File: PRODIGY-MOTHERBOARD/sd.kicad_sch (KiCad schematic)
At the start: 8 parts, among them J21 DM3BT-DSF-PEJS/C, Q2 DMP2045U-7, U17 IP4252CZ16

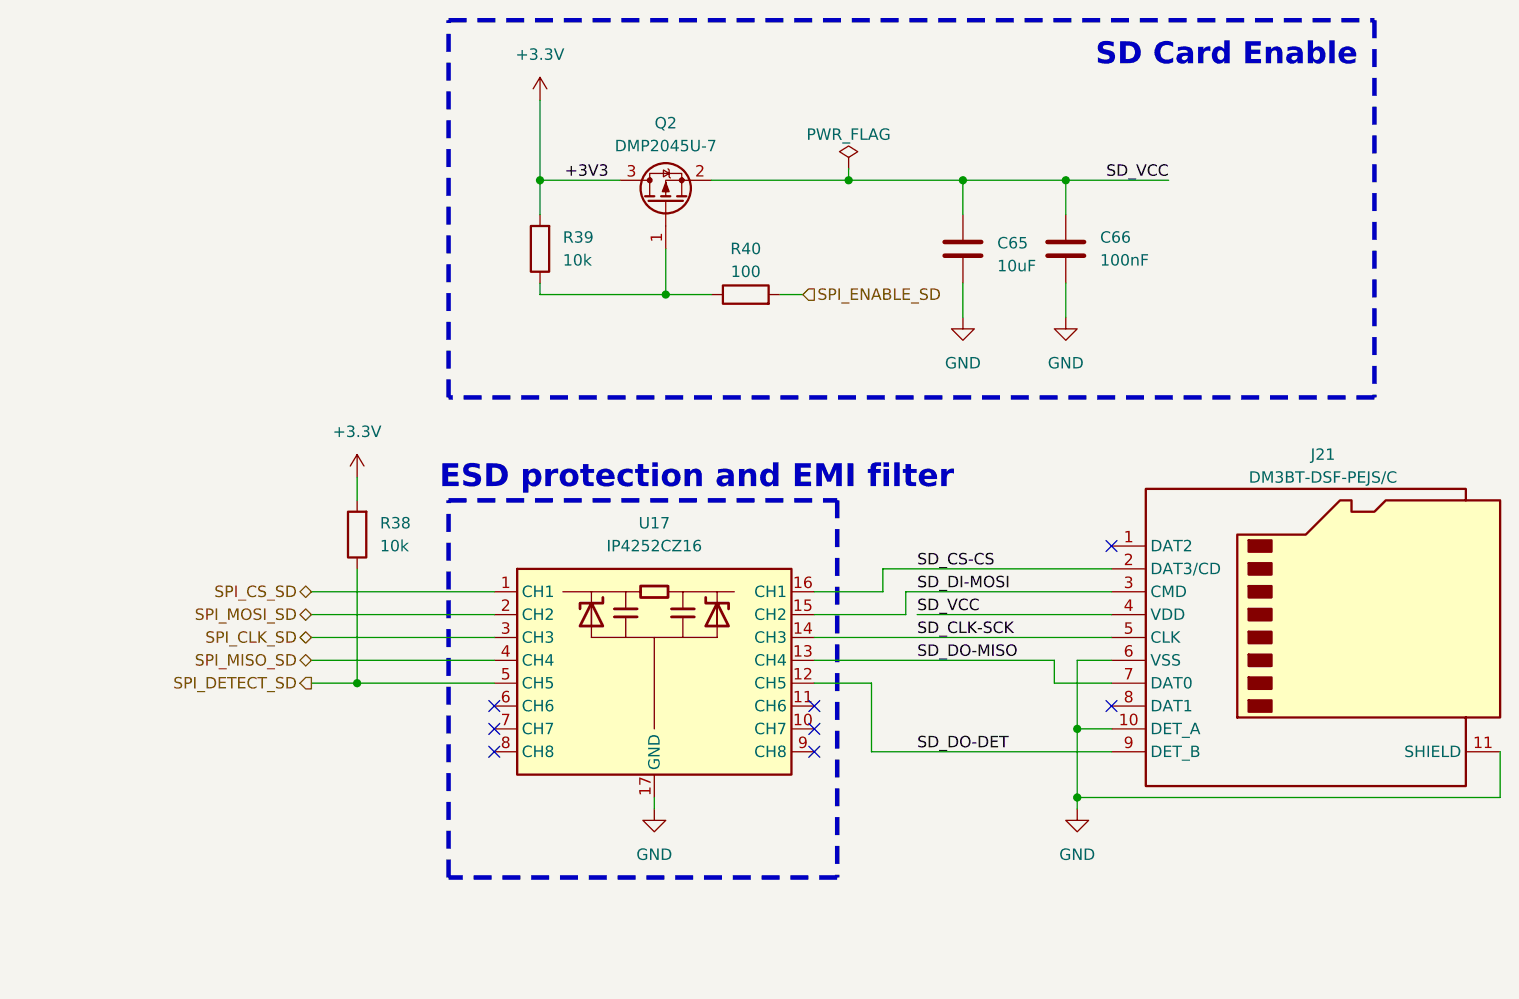
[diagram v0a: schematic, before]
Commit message: MBT Schematic improved
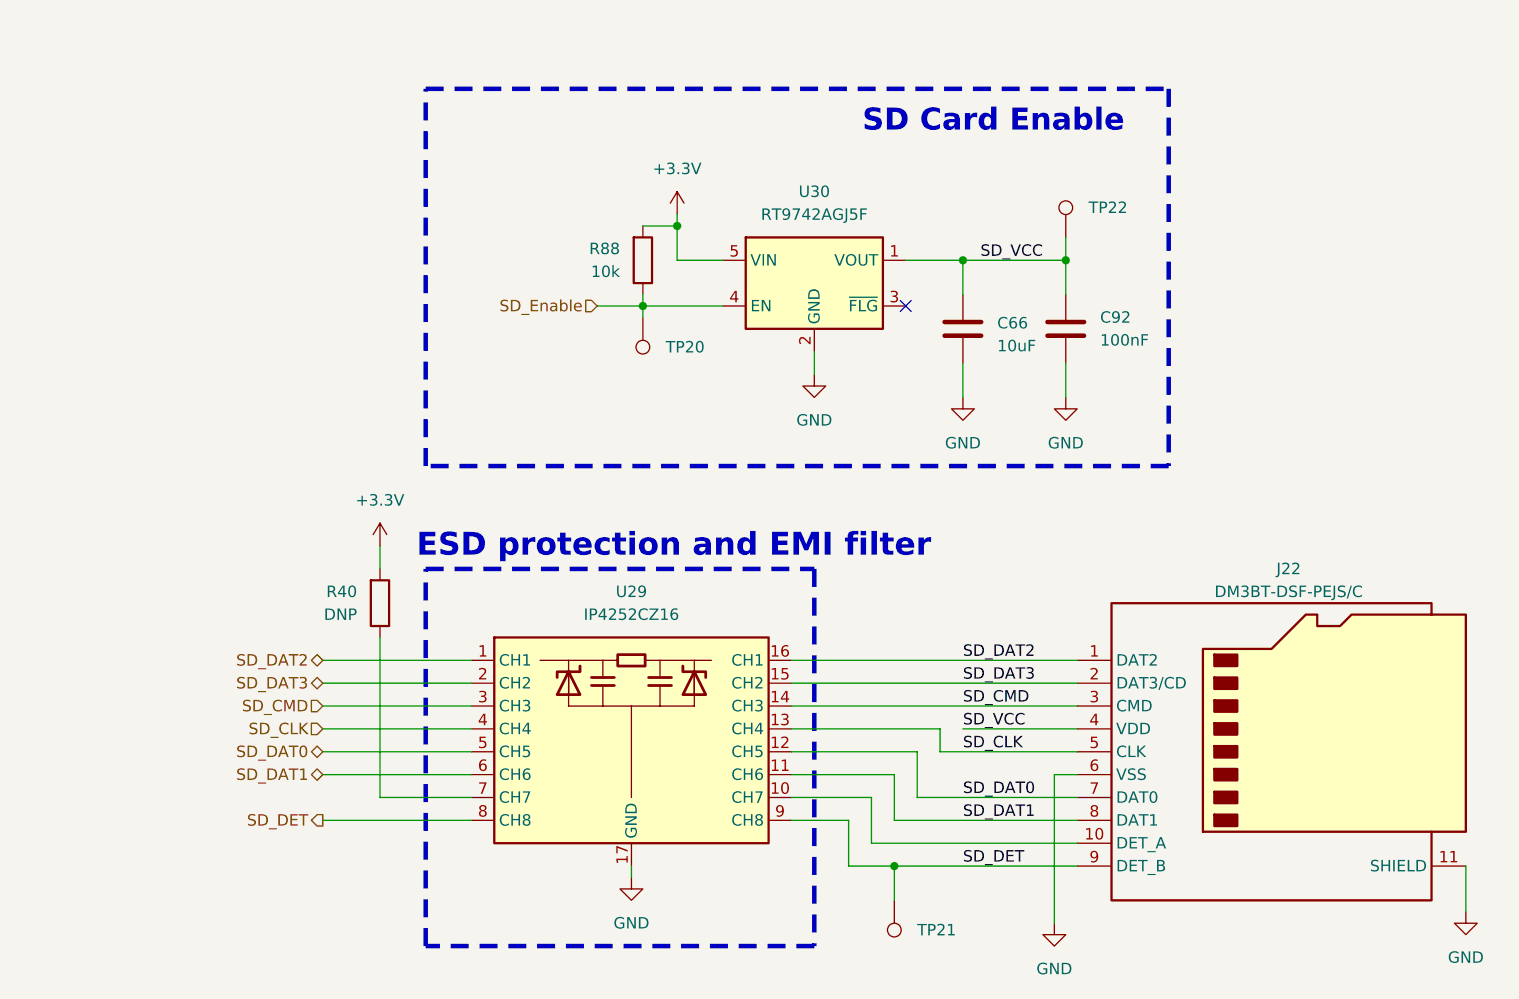
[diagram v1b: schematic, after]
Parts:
- removed C65: 10uF, Capacitor_SMD:C_1206_3216Metric, symbol Device:C
- removed J21: DM3BT-DSF-PEJS/C, Connector_Card:microSD_HC_Hirose_DM3BT-DSF-PEJS, symbol Connector:Micro_SD_Card_Det2
- removed Q2: DMP2045U-7, Package_TO_SOT_SMD:SOT-23, symbol Transistor_FET:IRLML6402
- removed R38, R39: 10k, Resistor_SMD:R_0603_1608Metric, symbol Device:R
- removed U17: IP4252CZ16, Package_SON:Nexperia_HUSON-16_USON-16-1EP_1.35x3.3mm_P0.4mm_EP0.4x2.8mm, symbol Power_Protection:IP4252CZ16
- added C92: 100nF, Capacitor_SMD:C_0805_2012Metric, symbol Device:C
- added J22: DM3BT-DSF-PEJS/C, Connector_Card:microSD_HC_Hirose_DM3BT-DSF-PEJS, symbol Connector:Micro_SD_Card_Det2
- added R88: 10k, Resistor_SMD:R_0603_1608Metric, symbol Device:R
- added TP20, TP21, TP22: ~, TestPoint:TestPoint_Pad_D3.0mm, symbol Connector:TestPoint
- added U29: IP4252CZ16, Package_SON:Nexperia_HUSON-16_USON-16-1EP_1.35x3.3mm_P0.4mm_EP0.4x2.8mm, symbol Power_Protection:IP4252CZ16
- added U30: RT9742AGJ5F, Package_TO_SOT_SMD:TSOT-23-5, symbol Power_Management:RT9742AGJ5F
- C66: value 100nF -> 10uF; footprint Capacitor_SMD:C_0805_2012Metric -> Capacitor_SMD:C_1206_3216Metric
- R40: value 100 -> DNP
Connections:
- net SPI_ENABLE_SD is gone; now on net +3.3V: R40.2
- net +3.3V: now also R88.2, U30.5 (VIN)
- net GND: now also C92.2, J22.11 (SHIELD), J22.6 (VSS), U29.17 (GND), U30.2 (GND)
- net SD_VCC: now also C92.1, J22.4 (VDD), TP22.1, U30.1 (VOUT)
- net at R40.1: now also U29.7 (CH7)
- new net: J22.10 (DET_A), U29.10 (CH7)
- new net SD_CLK: J22.5 (CLK), U29.13 (CH4), U29.4 (CH4)
- new net SD_CMD: J22.3 (CMD), U29.14 (CH3), U29.3 (CH3)
- new net SD_DAT0: J22.7 (DAT0), U29.12 (CH5), U29.5 (CH5)
- new net SD_DAT1: J22.8 (DAT1), U29.11 (CH6), U29.6 (CH6)
- new net SD_DAT2: J22.1 (DAT2), U29.1 (CH1), U29.16 (CH1)
- new net SD_DAT3: J22.2 (DAT3/CD), U29.15 (CH2), U29.2 (CH2)
- new net SD_DET: J22.9 (DET_B), TP21.1, U29.8 (CH8), U29.9 (CH8)
- new net SD_Enable: R88.1, TP20.1, U30.4 (EN)
- no-connect marks 8 -> 1

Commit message: schematic v0.2 finalized
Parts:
- renumbered C66 to C89, C92 to C90, J22 to J21, R40 to R85, R88 to R86, TP20 to TP17, TP21 to TP18, TP22 to TP19, U29 to U27, U30 to U28
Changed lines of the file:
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@@
 		(dnp no)
 		(fields_autoplaced yes)
-		(property "Reference" "U29"
+		(property "Reference" "U27"
 			(at 120.65 104.14 0)
 			(effects
@@
 			(project "PRODIGY-MOTHERBOARD"
 				(path "/f1c25860-8989-4190-bd24-2491d23ca7d9/20646931-b26f-4e3f-9f16-a00d92b20b98"
-					(reference "U29")
+					(reference "U27")
 					(unit 1)
 				)
@@
 		(on_board yes)
 		(dnp no)
-		(property "Reference" "TP21"
+		(property "Reference" "TP18"
 			(at 152.4 141.7319 0)
 			(effects
@@
 			(project "PRODIGY-MOTHERBOARD"
 				(path "/f1c25860-8989-4190-bd24-2491d23ca7d9/20646931-b26f-4e3f-9f16-a00d92b20b98"
-					(reference "TP21")
+					(reference "TP18")
 					(unit 1)
 				)
@@
 		(dnp no)
 		(fields_autoplaced yes)
-		(property "Reference" "#PWR0253"
+		(property "Reference" "#PWR0249"
 			(at 120.65 142.24 0)
 			(effects
@@
 			(project "PRODIGY-MOTHERBOARD"
 				(path "/f1c25860-8989-4190-bd24-2491d23ca7d9/20646931-b26f-4e3f-9f16-a00d92b20b98"
-					(reference "#PWR0253")
+					(reference "#PWR0249")
 					(unit 1)
 				)
@@
 		(on_board yes)
 		(dnp no)
-		(property "Reference" "R88"
+		(property "Reference" "R86"
 			(at 119.38 66.0399 0)
 			(effects
@@
 			(project "PRODIGY-MOTHERBOARD"
 				(path "/f1c25860-8989-4190-bd24-2491d23ca7d9/20646931-b26f-4e3f-9f16-a00d92b20b98"
-					(reference "R88")
+					(reference "R86")
 					(unit 1)
 				)
@@
 		(dnp no)
 		(fields_autoplaced yes)
-		(property "Reference" "#PWR0256"
+		(property "Reference" "#PWR0252"
 			(at 157.48 88.9 0)
 			(effects
@@
 			(project "PRODIGY-MOTHERBOARD"
 				(path "/f1c25860-8989-4190-bd24-2491d23ca7d9/20646931-b26f-4e3f-9f16-a00d92b20b98"
-					(reference "#PWR0256")
+					(reference "#PWR0252")
 					(unit 1)
 				)
@@
 		(dnp no)
 		(fields_autoplaced yes)
-		(property "Reference" "U30"
+		(property "Reference" "U28"
 			(at 140.97 59.69 0)
 			(effects
@@
 			(project "PRODIGY-MOTHERBOARD"
 				(path "/f1c25860-8989-4190-bd24-2491d23ca7d9/20646931-b26f-4e3f-9f16-a00d92b20b98"
-					(reference "U30")
+					(reference "U28")
 					(unit 1)
 				)
@@
 		(dnp no)
 		(fields_autoplaced yes)
-		(property "Reference" "#PWR0252"
+		(property "Reference" "#PWR0248"
 			(at 92.71 102.87 0)
 			(effects
@@
 			(project "PRODIGY-MOTHERBOARD"
 				(path "/f1c25860-8989-4190-bd24-2491d23ca7d9/20646931-b26f-4e3f-9f16-a00d92b20b98"
-					(reference "#PWR0252")
+					(reference "#PWR0248")
 					(unit 1)
 				)
@@
 		(dnp no)
 		(fields_autoplaced yes)
-		(property "Reference" "TP22"
+		(property "Reference" "TP19"
 			(at 171.45 61.4679 0)
 			(effects
@@
 			(project "PRODIGY-MOTHERBOARD"
 				(path "/f1c25860-8989-4190-bd24-2491d23ca7d9/20646931-b26f-4e3f-9f16-a00d92b20b98"
-					(reference "TP22")
+					(reference "TP19")
 					(unit 1)
 				)
@@
 		(dnp no)
 		(fields_autoplaced yes)
-		(property "Reference" "#PWR0254"
+		(property "Reference" "#PWR0250"
 			(at 125.73 66.04 0)
 			(effects
@@
 			(project "PRODIGY-MOTHERBOARD"
 				(path "/f1c25860-8989-4190-bd24-2491d23ca7d9/20646931-b26f-4e3f-9f16-a00d92b20b98"
-					(reference "#PWR0254")
+					(reference "#PWR0250")
 					(unit 1)
 				)
@@
 		(dnp no)
 		(fields_autoplaced yes)
-		(property "Reference" "C66"
+		(property "Reference" "C89"
 			(at 161.29 74.295 0)
 			(effects
@@
 			(project "PRODIGY-MOTHERBOARD"
 				(path "/f1c25860-8989-4190-bd24-2491d23ca7d9/20646931-b26f-4e3f-9f16-a00d92b20b98"
-					(reference "C66")
+					(reference "C89")
 					(unit 1)
 				)
@@
 		(dnp no)
 		(fields_autoplaced yes)
-		(property "Reference" "#PWR0258"
+		(property "Reference" "#PWR0254"
 			(at 168.91 88.9 0)
 			(effects
@@
 			(project "PRODIGY-MOTHERBOARD"
 				(path "/f1c25860-8989-4190-bd24-2491d23ca7d9/20646931-b26f-4e3f-9f16-a00d92b20b98"
-					(reference "#PWR0258")
+					(reference "#PWR0254")
 					(unit 1)
 				)
@@
 		(on_board yes)
 		(dnp no)
-		(property "Reference" "TP20"
+		(property "Reference" "TP17"
 			(at 124.46 76.9621 0)
 			(effects
@@
 			(project "PRODIGY-MOTHERBOARD"
 				(path "/f1c25860-8989-4190-bd24-2491d23ca7d9/20646931-b26f-4e3f-9f16-a00d92b20b98"
-					(reference "TP20")
+					(reference "TP17")
 					(unit 1)
 				)
@@
 		(dnp no)
 		(fields_autoplaced yes)
-		(property "Reference" "#PWR0257"
+		(property "Reference" "#PWR0253"
 			(at 167.64 147.32 0)
 			(effects
@@
 			(project "PRODIGY-MOTHERBOARD"
 				(path "/f1c25860-8989-4190-bd24-2491d23ca7d9/20646931-b26f-4e3f-9f16-a00d92b20b98"
-					(reference "#PWR0257")
+					(reference "#PWR0253")
 					(unit 1)
 				)
@@
 		(on_board yes)
 		(dnp no)
-		(property "Reference" "J22"
+		(property "Reference" "J21"
 			(at 193.675 101.6 0)
 			(effects
@@
 			(project "PRODIGY-MOTHERBOARD"
 				(path "/f1c25860-8989-4190-bd24-2491d23ca7d9/20646931-b26f-4e3f-9f16-a00d92b20b98"
-					(reference "J22")
+					(reference "J21")
 					(unit 1)
 				)
@@
 		(dnp no)
 		(fields_autoplaced yes)
-		(property "Reference" "#PWR0255"
+		(property "Reference" "#PWR0251"
 			(at 140.97 86.36 0)
 			(effects
@@
 			(project "PRODIGY-MOTHERBOARD"
 				(path "/f1c25860-8989-4190-bd24-2491d23ca7d9/20646931-b26f-4e3f-9f16-a00d92b20b98"
-					(reference "#PWR0255")
+					(reference "#PWR0251")
 					(unit 1)
 				)
@@
 		(on_board yes)
 		(dnp no)
-		(property "Reference" "R40"
+		(property "Reference" "R85"
 			(at 90.17 104.1399 0)
 			(effects
@@
 			(project "PRODIGY-MOTHERBOARD"
 				(path "/f1c25860-8989-4190-bd24-2491d23ca7d9/20646931-b26f-4e3f-9f16-a00d92b20b98"
-					(reference "R40")
+					(reference "R85")
 					(unit 1)
 				)
@@
 		(dnp no)
 		(fields_autoplaced yes)
-		(property "Reference" "#PWR0259"
+		(property "Reference" "#PWR0255"
 			(at 213.36 146.05 0)
 			(effects
@@
 			(project "PRODIGY-MOTHERBOARD"
 				(path "/f1c25860-8989-4190-bd24-2491d23ca7d9/20646931-b26f-4e3f-9f16-a00d92b20b98"
-					(reference "#PWR0259")
+					(reference "#PWR0255")
 					(unit 1)
 				)
@@
 		(dnp no)
 		(fields_autoplaced yes)
-		(property "Reference" "C92"
+		(property "Reference" "C90"
 			(at 172.72 73.6599 0)
 			(effects
@@
 			(project "PRODIGY-MOTHERBOARD"
 				(path "/f1c25860-8989-4190-bd24-2491d23ca7d9/20646931-b26f-4e3f-9f16-a00d92b20b98"
-					(reference "C92")
-					(unit 1)
-				)
+					(reference "C90")
+					(unit 1)
+				)

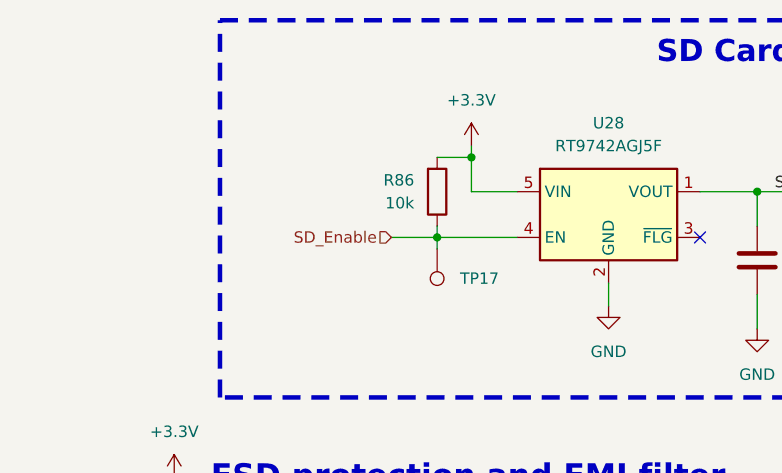
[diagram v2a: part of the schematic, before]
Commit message: Motherboard footprints assigned.
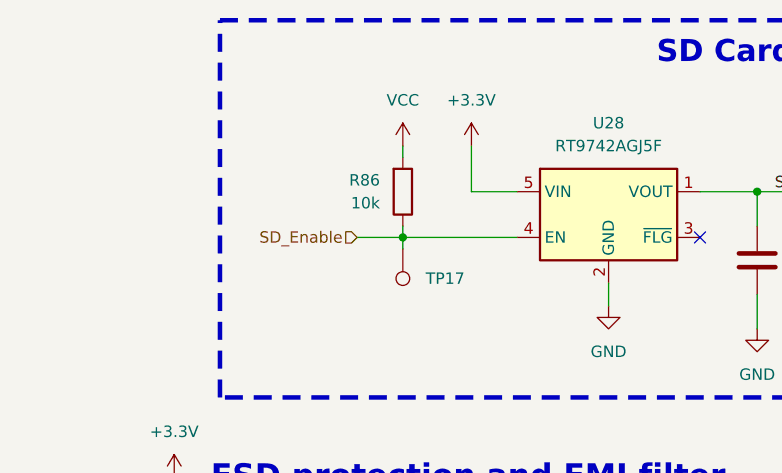
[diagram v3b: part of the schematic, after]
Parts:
- C89: footprint Capacitor_SMD:C_1206_3216Metric -> Capacitor_SMD:C_0805_2012Metric
- C90: footprint Capacitor_SMD:C_0805_2012Metric -> Capacitor_SMD:C_0603_1608Metric
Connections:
- net +3.3V: no longer R86.2
- new net VCC: R86.2
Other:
- moved on the sheet: R86, TP17

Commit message: finished motherboard bom and updated footprints
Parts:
- added RN6: 10k, Resistor_SMD:R_0603_1608Metric, symbol Device:R_Network04
- C89: TME (none) -> CL21A106KOQNNNE
- C90: TME (none) -> CL10B104KB8NNNC
- J21: TME (none) -> DM3BT-DSF-PEJS/C
- R85: value DNP -> 10k; now not fitted
- R86: TME (none) -> WR06X1002FTL
- TP17, TP18, TP19: now not fitted
- U27: MOUSER (none) -> 771-IP4252CZ168TTL1
- U28: MOUSER (none) -> 835-RT9742AGJ5F
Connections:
- net SD_DAT0: now also RN6.4 (R3)
- net SD_DAT1: now also RN6.5 (R4)
- net SD_DAT2: now also RN6.2 (R1)
- net SD_DAT3: now also RN6.3 (R2)
- net VCC: now also RN6.1 (common)

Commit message: Motherboard PCB layout started
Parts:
- RN6: footprint Resistor_SMD:R_0603_1608Metric -> Resistor_SMD:R_Array_Convex_4x0603
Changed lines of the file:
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@@
 			)
 		)
-		(property "Footprint" "Resistor_SMD:R_0603_1608Metric"
+		(property "Footprint" "Resistor_SMD:R_Array_Convex_4x0603"
 			(at 84.455 104.14 90)
 			(effects

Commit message: Analog lazout done
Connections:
- net SD_DAT0: now also RN6.3 (R2); no longer RN6.4 (R3)
- net SD_DAT1: now also RN6.2 (R1); no longer RN6.5 (R4)
- net SD_DAT2: now also RN6.5 (R4); no longer RN6.2 (R1)
- net SD_DAT3: now also RN6.4 (R3); no longer RN6.3 (R2)
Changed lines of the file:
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@@
 	(wire
 		(pts
-			(xy 72.39 97.79) (xy 72.39 99.06)
+			(xy 80.01 97.79) (xy 80.01 99.06)
 		)
 		(stroke
@@
 				(path "/f1c25860-8989-4190-bd24-2491d23ca7d9/20646931-b26f-4e3f-9f16-a00d92b20b98"
 					(reference "#PWR0250")
-					(unit 1)
-				)
-			)
-		)
-	)
-	(symbol
-		(lib_id "Device:R_Network04")
-		(at 77.47 104.14 0)
-		(unit 1)
-		(exclude_from_sim no)
-		(in_bom yes)
-		(on_board yes)
-		(dnp yes)
-		(property "Reference" "RN6"
-			(at 69.85 103.1239 0)
-			(effects
-				(font
-					(size 1.27 1.27)
-				)
-				(justify right)
-			)
-		)
-		(property "Value" "10k"
-			(at 69.85 105.6639 0)
-			(effects
-				(font
-					(size 1.27 1.27)
-				)
-				(justify right)
-			)
-		)
-		(property "Footprint" "Resistor_SMD:R_Array_Convex_4x0603"
-			(at 84.455 104.14 90)
-			(effects
-				(font
-					(size 1.27 1.27)
-				)
-				(hide yes)
-			)
-		)
-		(property "Datasheet" "http://www.vishay.com/docs/31509/csc.pdf"
-			(at 77.47 104.14 0)
-			(effects
-				(font
-					(size 1.27 1.27)
-				)
-				(hide yes)
-			)
-		)
-		(property "Description" "4 resistor network, star topology, bussed resistors, small symbol"
-			(at 77.47 104.14 0)
-			(effects
-				(font
-					(size 1.27 1.27)
-				)
-				(hide yes)
-			)
-		)
-		(property "MOUSER" ""
-			(at 77.47 104.14 0)
-			(effects
-				(font
-					(size 1.27 1.27)
-				)
-				(hide yes)
-			)
-		)
-		(property "Sim.Type" ""
-			(at 77.47 104.14 0)
-			(effects
-				(font
-					(size 1.27 1.27)
-				)
-				(hide yes)
-			)
-		)
-		(property "TME" ""
-			(at 77.47 104.14 0)
-			(effects
-				(font
-					(size 1.27 1.27)
-				)
-				(hide yes)
-			)
-		)
-		(pin "2"
-		)
-		(pin "4"
-		)
-		(pin "3"
-		)
-		(pin "1"
-		)
-		(pin "5"
-		)
-		(instances
-			(project "PRODIGY-MOTHERBOARD"
-				(path "/f1c25860-8989-4190-bd24-2491d23ca7d9/20646931-b26f-4e3f-9f16-a00d92b20b98"
-					(reference "RN6")
 					(unit 1)
 				)
@@
 	(symbol
 		(lib_id "power:VCC")
-		(at 72.39 97.79 0)
+		(at 80.01 97.79 0)
 		(unit 1)
 		(exclude_from_sim no)
@@
 		(fields_autoplaced yes)
 		(property "Reference" "#PWR0257"
-			(at 72.39 101.6 0)
+			(at 80.01 101.6 0)
 			(effects
 				(font
@@
 		)
 		(property "Value" "VCC"
-			(at 72.39 92.71 0)
+			(at 80.01 92.71 0)
 			(effects
 				(font
@@
 		)
 		(property "Footprint" ""
-			(at 72.39 97.79 0)
+			(at 80.01 97.79 0)
 			(effects
 				(font
@@
 		)
 		(property "Datasheet" ""
-			(at 72.39 97.79 0)
+			(at 80.01 97.79 0)
 			(effects
 				(font
@@
 		)
 		(property "Description" "Power symbol creates a global label with name \"VCC\""
-			(at 72.39 97.79 0)
+			(at 80.01 97.79 0)
 			(effects
 				(font
@@
 					(unit 1)
 				)
+			)
+		)
+	)
+	(symbol
+		(lib_id "Device:R_Network04")
+		(at 74.93 104.14 0)
+		(mirror y)
+		(unit 1)
+		(exclude_from_sim no)
+		(in_bom yes)
+		(on_board yes)
+		(dnp yes)
+		(property "Reference" "RN6"
+			(at 82.55 103.1239 0)
+			(effects
+				(font
+					(size 1.27 1.27)
+				)
+				(justify right)
+			)
+		)
+		(property "Value" "10k"
+			(at 82.55 105.6639 0)
+			(effects
+				(font
+					(size 1.27 1.27)
+				)
+				(justify right)
+			)
+		)
+		(property "Footprint" "Resistor_SMD:R_Array_Convex_4x0603"
+			(at 67.945 104.14 90)
+			(effects
+				(font
+					(size 1.27 1.27)
+				)
+				(hide yes)
+			)
+		)
+		(property "Datasheet" "http://www.vishay.com/docs/31509/csc.pdf"
+			(at 74.93 104.14 0)
+			(effects
+				(font
+					(size 1.27 1.27)
+				)
+				(hide yes)
+			)
+		)
+		(property "Description" "4 resistor network, star topology, bussed resistors, small symbol"
+			(at 74.93 104.14 0)
+			(effects
+				(font
+					(size 1.27 1.27)
+				)
+				(hide yes)
+			)
+		)
+		(property "MOUSER" ""
+			(at 74.93 104.14 0)
+			(effects
+				(font
+					(size 1.27 1.27)
+				)
+				(hide yes)
+			)
+		)
+		(property "Sim.Type" ""
+			(at 74.93 104.14 0)
+			(effects
+				(font
+					(size 1.27 1.27)
+				)
+				(hide yes)
+			)
+		)
+		(property "TME" ""
+			(at 74.93 104.14 0)
+			(effects
+				(font
+					(size 1.27 1.27)
+				)
+				(hide yes)
+			)
+		)
+		(pin "2"
+		)
+		(pin "4"
+		)
+		(pin "3"
+		)
+		(pin "1"
+		)
+		(pin "5"
+		)
+		(instances
+			(project "PRODIGY-MOTHERBOARD"
+				(path "/f1c25860-8989-4190-bd24-2491d23ca7d9/20646931-b26f-4e3f-9f16-a00d92b20b98"
+					(reference "RN6")
+					(unit 1)
+				)
